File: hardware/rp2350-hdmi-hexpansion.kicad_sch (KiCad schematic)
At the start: 87 parts, among them J1 Hexpansion-Connector, J2 USB-C, J3 SWD, J4 Qwiic, J5 HDMI-A, SW1 BOOTSEL, SW3 RESET, U1 RP2354A, U10 ZD24C64A (fallback), U11 SN74LVC1G07, U2 TPS2116DRLR, U3 TLV62569DBVR, U4 TPS61023DRLR, U6 TPD4E05U06, U7 TPD4E05U06, U8 USBLC6-2SC6, U9 APS6404L-3SQR-SN, Y1 12MHz

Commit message: hardware: fix C13/C14 schematic symbols (lib_id pointed at a non-existent library symbol)
Co-Authored-By: Claude Sonnet 5.5 <noreply@anthropic.com>
Claude-Session: https://claude.ai/code/session_01VMD2iSg4JfioYFvgvvdo7j
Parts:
- C13, C14: symbol jlc:CL10A475KO8NNNC -> jlc:CL05A475MP5NRNC
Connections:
- net +3V3: now also C14.1
- net DVDD: now also C13.1
- net GND: now also C13.2, C14.2
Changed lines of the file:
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@@
 	)
 	(symbol
-		(lib_id "jlc:CL10A475KO8NNNC")
+		(lib_id "jlc:CL05A475MP5NRNC")
 		(at 189.23 193.04 0)
 		(unit 1)
@@
 	)
 	(symbol
-		(lib_id "jlc:CL10A475KO8NNNC")
+		(lib_id "jlc:CL05A475MP5NRNC")
 		(at 219.71 193.04 0)
 		(unit 1)

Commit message: hardware: merge 3V3_BADGE into +3V3, ignore hardware/reference, save PCB layout
Co-Authored-By: Claude Sonnet 5.5 <noreply@anthropic.com>
Claude-Session: https://claude.ai/code/session_01VMD2iSg4JfioYFvgvvdo7j
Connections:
- net 3V3_BADGE is gone; now on net +3V3: C23.1, C29.1, C33.1, J1.15 (3V3), J1.16 (3V3), R16.1, R4.1, R41.1, U10.8 (VCC), U11.5 (VCC), U2.6 (VIN2)
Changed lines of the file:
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@@
 		)
 	)
-	(label "3V3_BADGE"
+	(label "+3V3"
 		(at 96.52 289.56 0)
 		(effects
@@
 		)
 	)
-	(label "3V3_BADGE"
+	(label "+3V3"
 		(at 118.11 318.77 0)
 		(effects
@@
 		)
 	)
-	(label "3V3_BADGE"
+	(label "+3V3"
 		(at 328.93 52.07 0)
 		(effects
@@
 		)
 	)
-	(label "3V3_BADGE"
+	(label "+3V3"
 		(at 666.75 349.25 180)
 		(effects
@@
 		)
 	)
-	(label "3V3_BADGE"
+	(label "+3V3"
 		(at 328.93 52.07 0)
 		(effects
@@
 		)
 	)
-	(label "3V3_BADGE"
+	(label "+3V3"
 		(at 635 350.52 0)
 		(effects
@@
 		)
 	)
-	(label "3V3_BADGE"
+	(label "+3V3"
 		(at 96.52 300.99 0)
 		(effects
@@
 		)
 	)
-	(label "3V3_BADGE"
+	(label "+3V3"
 		(at 694.69 186.69 180)
 		(effects
@@
 		)
 	)
-	(label "3V3_BADGE"
+	(label "+3V3"
 		(at 353.06 52.07 180)
 		(effects
@@
 		)
 	)
-	(label "3V3_BADGE"
+	(label "+3V3"
 		(at 680.72 207.01 0)
 		(effects
@@
 		)
 	)
-	(label "3V3_BADGE"
+	(label "+3V3"
 		(at 665.48 186.69 0)
 		(effects

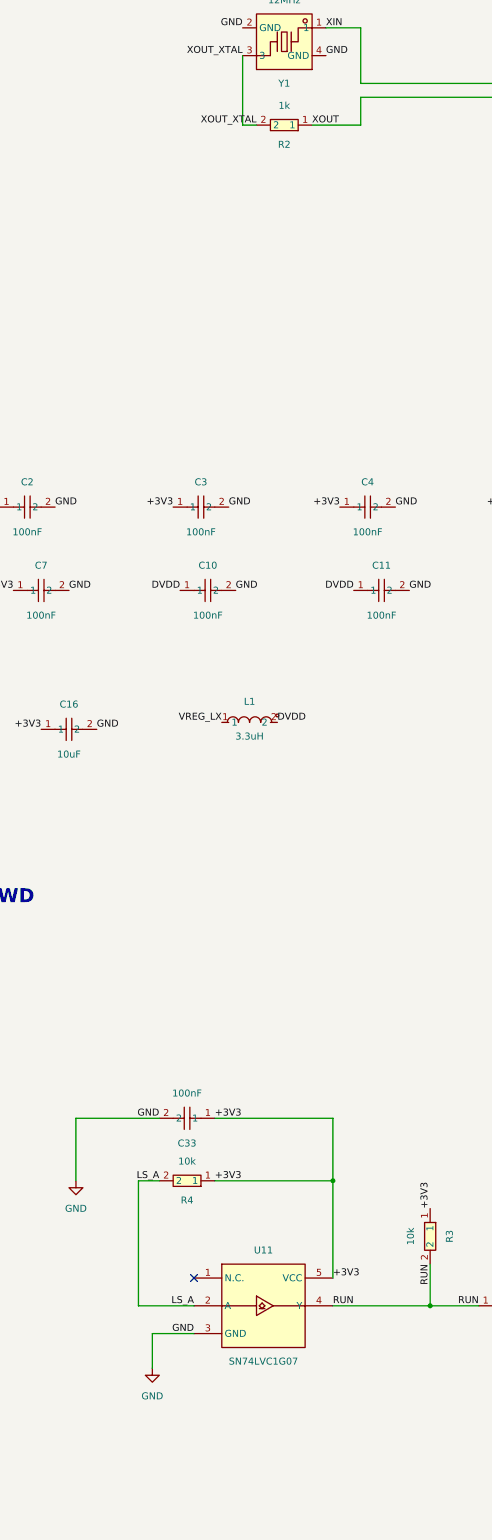
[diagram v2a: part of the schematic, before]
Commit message: hardware: drop U11/C33/R4, add R53 LS_A-RUN link, update PCB and BOM
Co-Authored-By: Claude Sonnet 5.5 <noreply@anthropic.com>
Claude-Session: https://claude.ai/code/session_01VMD2iSg4JfioYFvgvvdo7j
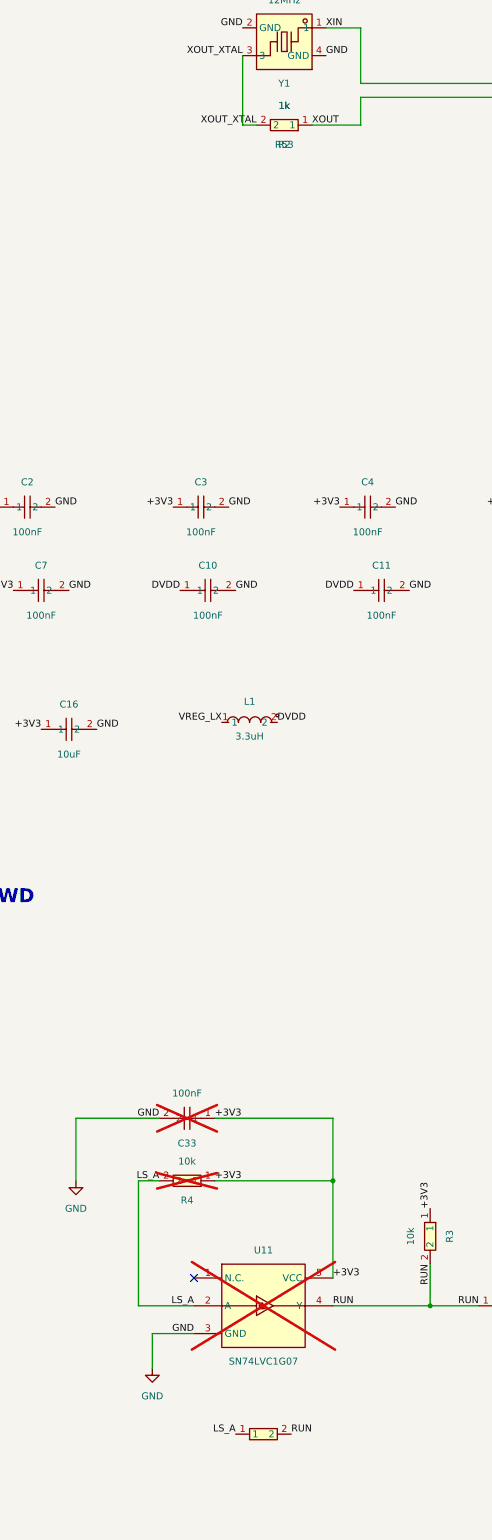
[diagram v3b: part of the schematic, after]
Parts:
- added R53: 1k, jlc:R0402, symbol jlc:0402WGF1001TCE
- C33, R4, U11: now not fitted; now left out of the parts list
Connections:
- net LS_A: now also R53.1
- net RUN: now also R53.2
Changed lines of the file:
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@@
 		)
 	)
+	(label "LS_A"
+		(at 100.33 347.32 180)
+		(effects
+			(font
+				(size 1.27 1.27)
+			)
+			(justify right bottom)
+		)
+	)
 	(label "SPI_CS"
 		(at 200.66 120.65 0)
@@
 		)
 	)
+	(label "RUN"
+		(at 110.49 347.32 0)
+		(effects
+			(font
+				(size 1.27 1.27)
+			)
+			(justify left bottom)
+		)
+	)
 	(label "GND"
 		(at 116.84 95.25 0)
@@
 		(body_style 1)
 		(exclude_from_sim no)
-		(in_bom yes)
-		(on_board yes)
+		(in_bom no)
+		(on_board no)
 		(in_pos_files yes)
-		(dnp no)
+		(dnp yes)
 		(property "Reference" "U11"
 			(at 105.41 313.69 0)
@@
 		(body_style 1)
 		(exclude_from_sim no)
-		(in_bom yes)
-		(on_board yes)
+		(in_bom no)
+		(on_board no)
 		(in_pos_files yes)
-		(dnp no)
+		(dnp yes)
 		(property "Reference" "C33"
 			(at 91.44 294.13 0)
@@
 		(body_style 1)
 		(exclude_from_sim no)
-		(in_bom yes)
-		(on_board yes)
+		(in_bom no)
+		(on_board no)
 		(in_pos_files yes)
-		(dnp no)
+		(dnp yes)
 		(property "Reference" "R4"
 			(at 91.44 304.55 0)
@@
 					(unit 1)
 				)
+			)
+		)
+	)
+	(symbol
+		(lib_id "jlc:0402WGF1001TCE")
+		(at 105.41 347.32 0)
+		(unit 1)
+		(body_style 1)
+		(exclude_from_sim no)
+		(in_bom yes)
+		(on_board yes)
+		(in_pos_files yes)
+		(dnp no)
+		(property "Reference" "R53"
+			(at 109.22 111.51 0)
+			(show_name no)
+			(do_not_autoplace no)
+			(effects
+				(font
+					(size 1.27 1.27)
+				)
+			)
+		)
+		(property "Value" "1k"
+			(at 109.22 104.39 0)
+			(show_name no)
+			(do_not_autoplace no)
+			(effects
+				(font
+					(size 1.27 1.27)
+				)
+			)
+		)
+		(property "Footprint" "jlc:R0402"
+			(at 109.22 107.95 0)
+			(hide yes)
+			(show_name no)
+			(do_not_autoplace no)
+			(effects
+				(font
+					(size 1.27 1.27)
+				)
+			)
+		)
+		(property "Datasheet" "https://lcsc.com/product-detail/Chip-Resistor-Surface-Mount-UniOhm_1KR-1001-1_C11702.html"
+			(at 109.22 107.95 0)
+			(hide yes)
+			(show_name no)
+			(do_not_autoplace no)
+			(effects
+				(font
+					(size 1.27 1.27)
+				)
+			)
+		)
+		(property "Description" ""
+			(at 109.22 107.95 0)
+			(show_name no)
+			(do_not_autoplace no)
+			(effects
+				(font
+					(size 1.27 1.27)
+				)
+			)
+		)
+		(property "Manufacturer" "UNI-ROYAL(厚声)"
+			(at 109.22 107.95 0)
+			(hide yes)
+			(show_name no)
+			(do_not_autoplace no)
+			(effects
+				(font
+					(size 1.27 1.27)
+				)
+			)
+		)
+		(property "MPN" "0402WGF1001TCE"
+			(at 109.22 107.95 0)
+			(hide yes)
+			(show_name no)
+			(do_not_autoplace no)
+			(effects
+				(font
+					(size 1.27 1.27)
+				)
+			)
+		)
+		(property "LCSC Part" "C11702"
+			(at 109.22 107.95 0)
+			(hide yes)
+			(show_name no)
+			(do_not_autoplace no)
+			(effects
+				(font
+					(size 1.27 1.27)
+				)
+			)
+		)
+		(property "ki_keywords" "Resistors"
+			(at 109.22 107.95 0)
+			(hide yes)
+			(show_name no)
+			(do_not_autoplace no)
+			(effects
+				(font
+					(size 1.27 1.27)
+				)
+			)
+		)
+		(property "ki_description" "1KΩ (1001) ±1%"
+			(at 109.22 107.95 0)
+			(hide yes)
+			(show_name no)
+			(do_not_autoplace no)
+			(effects
+				(font
+					(size 1.27 1.27)
+				)
+			)
+		)
+		(pin "1"
+		)
+		(pin "2"
+		)
+		(instances
+			(project "rp2350-hdmi-hexpansion"
+				(path "/fb9bfa6e-c44d-469c-aa90-8ec28bcdf17f"
+					(reference "R53")
+					(unit 1)
+				)
